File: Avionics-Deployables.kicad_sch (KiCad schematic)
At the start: 21 parts, among them J1 200528-0100

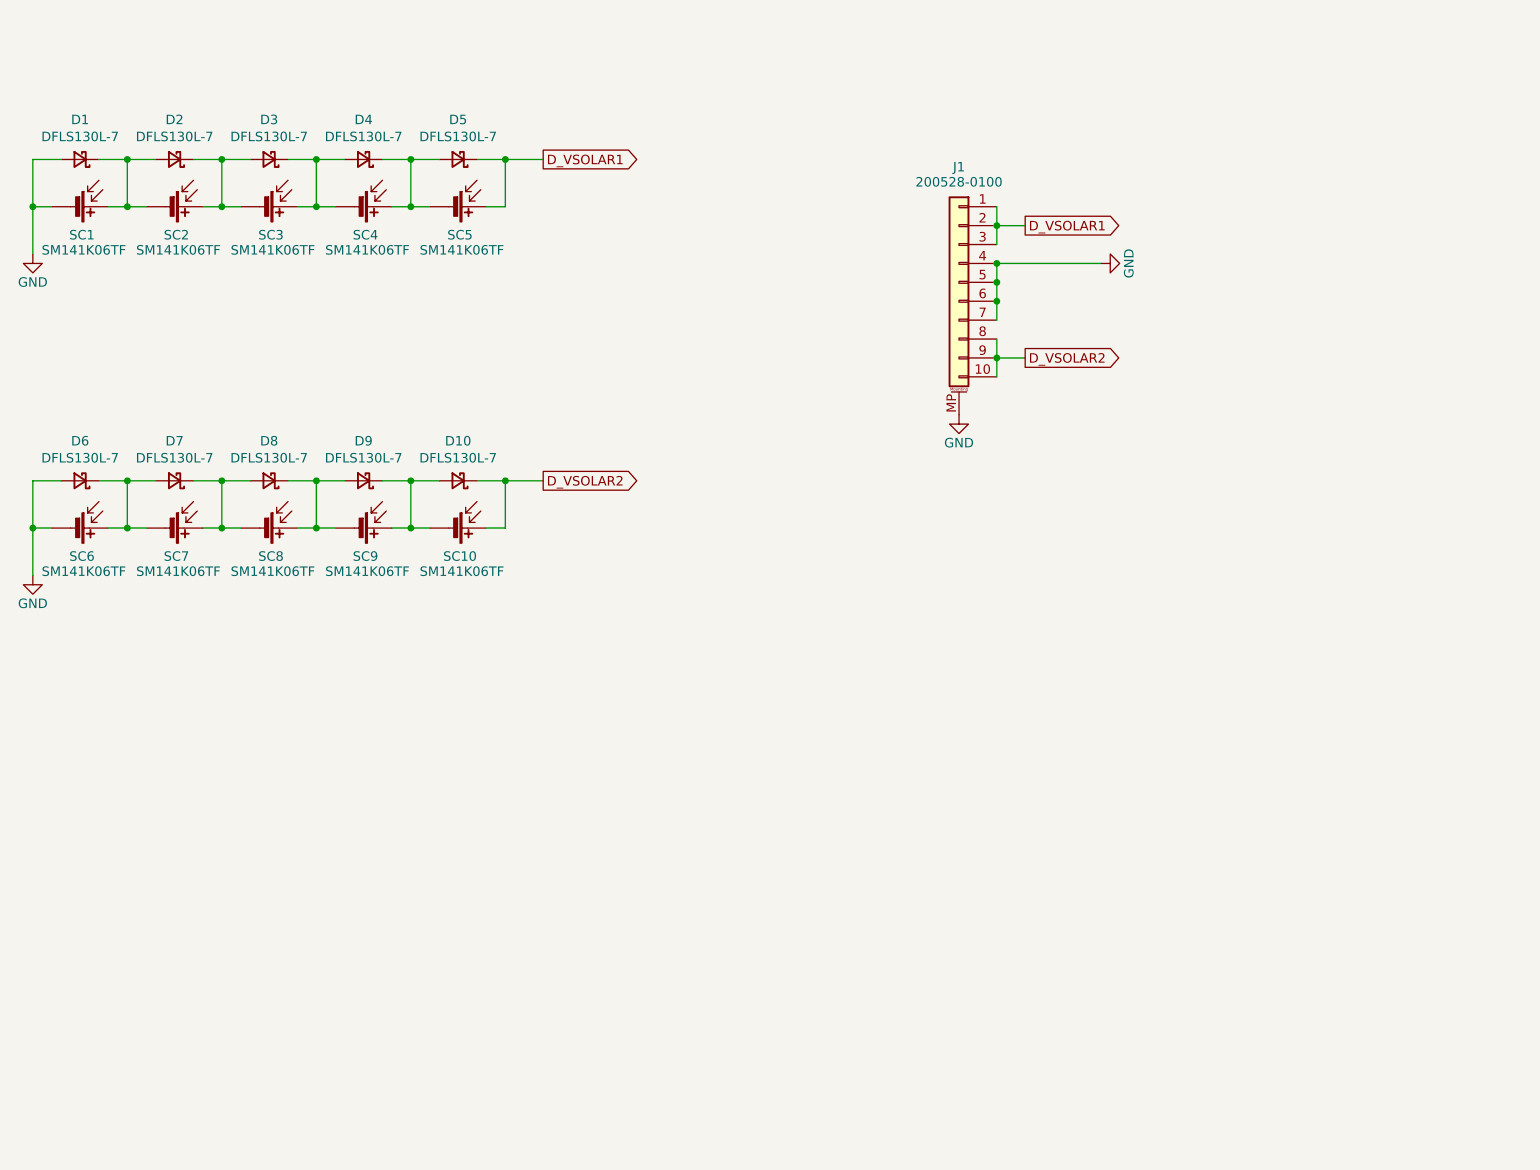
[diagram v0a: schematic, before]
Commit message: Update solar cell footprints
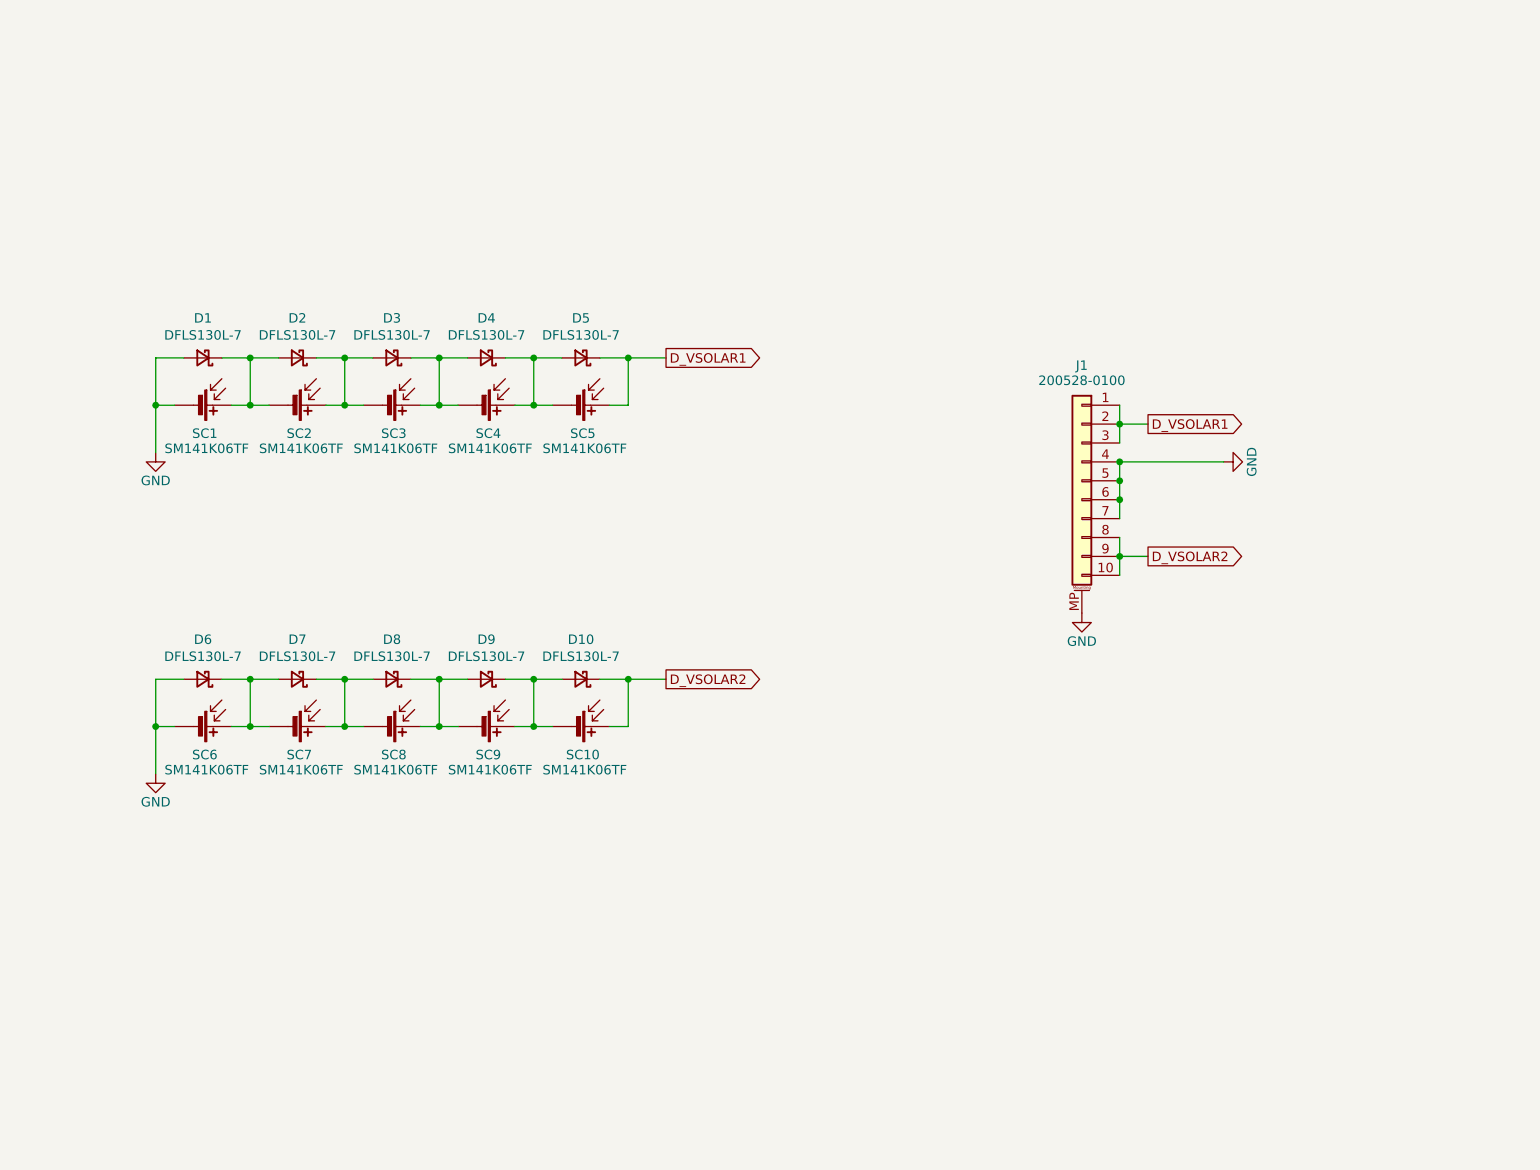
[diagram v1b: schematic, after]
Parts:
- SC1, SC10, SC2, SC3, SC4, SC5, SC6, SC7, SC8, SC9: footprint SolarPanels:SM141K06TF -> SolarPanels:SM141K06TF-S
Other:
- company: (none) -> Carnegie Mellon University
- title: (none) -> Argus Deployables
- moved on the sheet: D1, D10, D2, D3, D4, D5, D6, D7, D8, D9, J1, SC1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

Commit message: Exported BOM and STEP files
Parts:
- SC1, SC10, SC2, SC3, SC4, SC5, SC6, SC7, SC8, SC9: value SM141K06TF -> SM141K06TF/S
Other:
- note added: "The AnySolar SM141K06TF and SM141K06TFS variants are both usable the SM141K06TFVx variants are NOT"
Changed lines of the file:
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@@
+		)
+	)
+	(text "The AnySolar SM141K06TF and SM141K06TFS \nvariants are both usable\nthe SM141K06TFVx variants are NOT"
+		(exclude_from_sim no)
+		(at 80.01 102.616 0)
+		(effects
+			(font
+				(size 1.524 1.524)
+			)
+			(justify left)
 		)
 	)
@@
 			)
 		)
-		(property "Value" "SM141K06TF"
+		(property "Value" "SM141K06TF/S"
 			(at 102.108 131.572 90)
 			(effects
 				(font
-					(size 1.27 1.27)
+					(size 1.016 1.016)
 				)
 			)
@@
 			)
 		)
-		(property "Value" "SM141K06TF"
+		(property "Value" "SM141K06TF/S"
 			(at 102.108 88.392 90)
 			(effects
 				(font
-					(size 1.27 1.27)
+					(size 1.016 1.016)
 				)
 			)
@@
 			)
 		)
-		(property "Value" "SM141K06TF"
+		(property "Value" "SM141K06TF/S"
 			(at 89.408 131.572 90)
 			(effects
 				(font
-					(size 1.27 1.27)
+					(size 1.016 1.016)
 				)
 			)
@@
 			)
 		)
-		(property "Value" "SM141K06TF"
+		(property "Value" "SM141K06TF/S"
 			(at 89.408 88.392 90)
 			(effects
 				(font
-					(size 1.27 1.27)
+					(size 1.016 1.016)
 				)
 			)
@@
 			)
 		)
-		(property "Value" "SM141K06TF"
+		(property "Value" "SM141K06TF/S"
 			(at 114.808 131.572 90)
 			(effects
 				(font
-					(size 1.27 1.27)
+					(size 1.016 1.016)
 				)
 			)
@@
 			)
 		)
-		(property "Value" "SM141K06TF"
+		(property "Value" "SM141K06TF/S"
 			(at 76.708 131.572 90)
 			(effects
 				(font
-					(size 1.27 1.27)
+					(size 1.016 1.016)
 				)
 			)
@@
 			)
 		)
-		(property "Value" "SM141K06TF"
+		(property "Value" "SM141K06TF/S"
 			(at 76.708 88.392 90)
 			(effects
 				(font
-					(size 1.27 1.27)
+					(size 1.016 1.016)
 				)
 			)
@@
 			)
 		)
-		(property "Value" "SM141K06TF"
+		(property "Value" "SM141K06TF/S"
 			(at 127.508 88.392 90)
 			(effects
 				(font
-					(size 1.27 1.27)
+					(size 1.016 1.016)
 				)
 			)
@@
 			)
 		)
-		(property "Value" "SM141K06TF"
+		(property "Value" "SM141K06TF/S"
 			(at 127.508 131.572 90)
 			(effects
 				(font
-					(size 1.27 1.27)
+					(size 1.016 1.016)
 				)
 			)
@@
 			)
 		)
-		(property "Value" "SM141K06TF"
+		(property "Value" "SM141K06TF/S"
 			(at 114.808 88.392 90)
 			(effects
 				(font
-					(size 1.27 1.27)
-				)
-			)
+					(size 1.016 1.016)
+				)
+			)

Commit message: V3 Updates and Cell Backer
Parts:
- added H1, H10, H11, H12, H13, H14, H15, H16, H17, H18, H19, H2, H20, H3, H4, H5, H6, H7, H8, H9: MountingHole_Pad, TestPoint:TestPoint_Pad_D1.0mm, symbol Mechanical:MountingHole_Pad
- D1, D10, D2, D3, D4, D5, D6, D7, D8, D9: value DFLS130L-7 -> DFLS130LQ-7
- SC1, SC10, SC2, SC3, SC4, SC5, SC6, SC7, SC8, SC9: footprint SolarPanels:SM141K06TF-S -> Argus-Miscellaneous:SM141K06TF_S
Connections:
- net D_VSOLAR1: now also H8.1
- net D_VSOLAR2: now also H14.1
- net GND: now also H17.1, H18.1, H19.1, H20.1, H3.1, H9.1
- net at D8.1 (K), D9.2 (A), SC8.1 (+)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: now also H12.1
- net at D7.1 (K), D8.2 (A), SC7.1 (+)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: now also H11.1
- net at D6.1 (K), D7.2 (A), SC6.1 (+)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: now also H10.1, H15.1
- net at D3.1 (K), D4.2 (A), SC3.1 (+)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: now also H6.1
- net at D2.1 (K), D3.2 (A), SC2.1 (+)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: now also H5.1
- net at D1.1 (K), D2.2 (A), SC1.1 (+)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: now also H1.1, H4.1
- net at D10.2 (A), D9.1 (K), SC10.2 (-)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: now also H13.1, H16.1
- net at D4.1 (K), D5.2 (A), SC4.1 (+)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: now also H2.1, H7.1
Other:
- moved on the sheet: D1, D10, D2, D3, D4, D5, D6, D7, D8, D9, J1, SC1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
